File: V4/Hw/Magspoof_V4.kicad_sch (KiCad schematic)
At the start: 35 parts, among them J1 Coil, J2 SWD, P1 USB_C_Plug_USB2.0, Q1 DMG3415U-7, SW1 ON, SW3 S1, SW4 SOURCE MAG, SW5 RESET, U1 CH552G, U2 AP2112K-3.3, U3 TC4424, U5 MCP73831

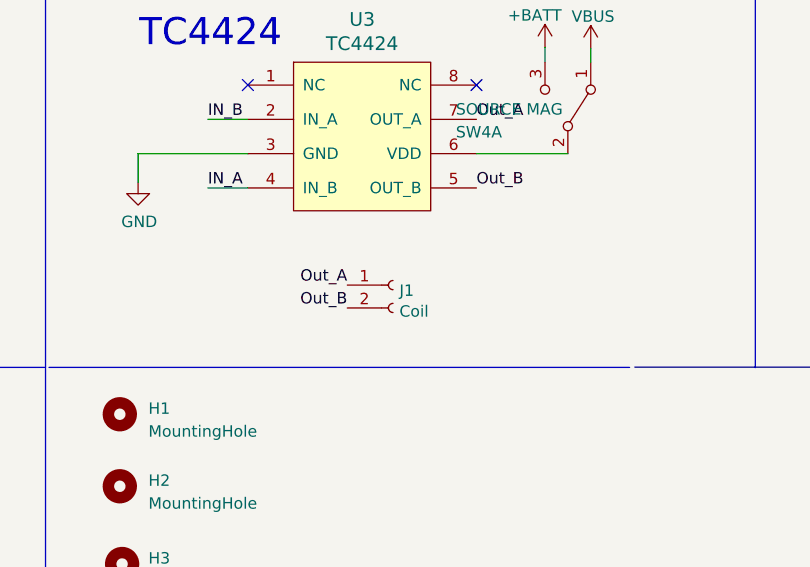
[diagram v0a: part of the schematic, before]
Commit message: feat: flat spiral coil proposals for PCB antenna
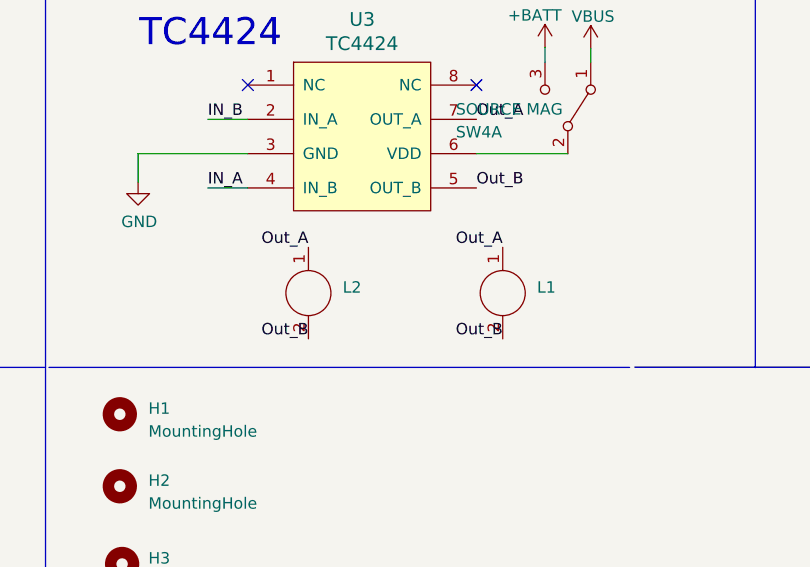
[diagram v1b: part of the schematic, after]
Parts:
- removed J1: Coil, Connector_PinHeader_2.54mm:PinHeader_1x02_P2.54mm_Vertical, symbol Connector:Conn_01x02_Female
- added L1: ~, Library:Coil_20t_35mm_0.2_0.2_0.6_0.3, symbol Magspoof:Coil_20t_35mm_0.2_0.6_0.3
- added L2: ~, magspoof:Coil_25t_30mm_0.2_0.2_0.6_0.3, symbol Magspoof:Coil_20t_35mm_0.2_0.6_0.3
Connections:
- net Out_A: now also L1.1, L2.1
- net Out_B: now also L1.2, L2.2

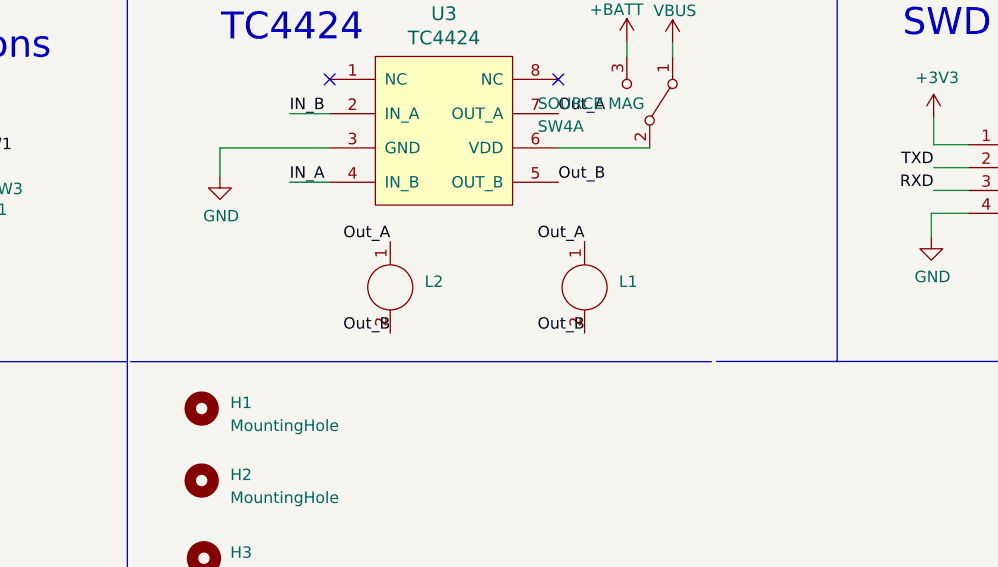
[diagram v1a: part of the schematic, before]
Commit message: feat(hw): add 2 additional coils and the specs of the coils
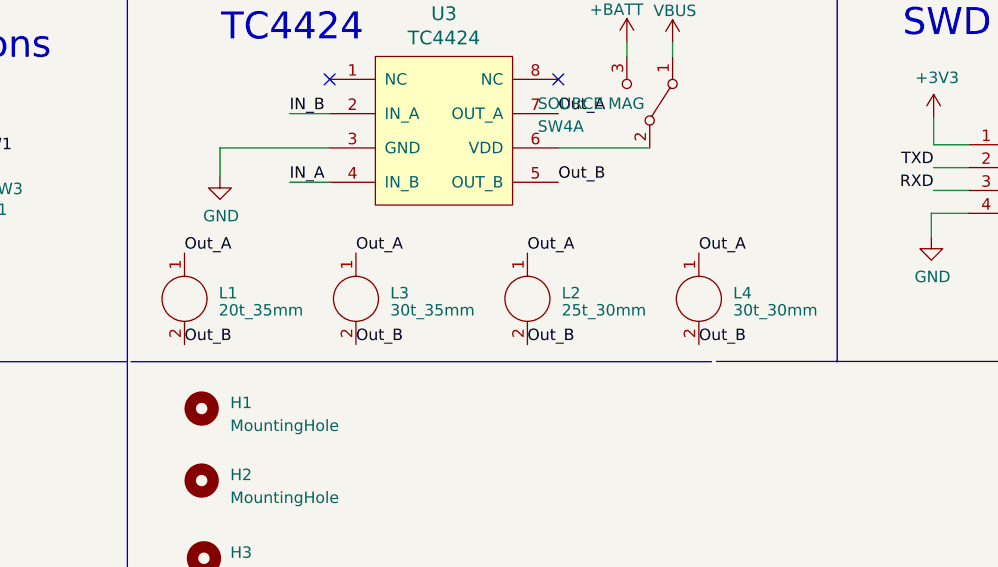
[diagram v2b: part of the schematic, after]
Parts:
- added L3: 30t_35mm, magspoof:Coil_30t_35mm_0.2_0.2_0.6_0.3, symbol Magspoof:Coil_20t_35mm_0.2_0.6_0.3
- added L4: 30t_30mm, magspoof:Coil_30t_30mm_0.2_0.2_0.6_0.3, symbol Magspoof:Coil_20t_35mm_0.2_0.6_0.3
- L1: value ~ -> 20t_35mm
- L2: value ~ -> 25t_30mm
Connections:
- net Out_A: now also L3.1, L4.1
- net Out_B: now also L3.2, L4.2
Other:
- moved on the sheet: L1, L2
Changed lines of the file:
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@@
 	)
 	(label "Out_B"
-		(at 210.82 99.06 180)
+		(at 226.06 100.33 0)
 		(fields_autoplaced yes)
 		(effects
@@
 				(size 1.27 1.27)
 			)
-			(justify right bottom)
+			(justify left bottom)
 		)
 	)
 	(label "Out_A"
-		(at 210.82 88.9 180)
+		(at 226.06 90.17 0)
 		(fields_autoplaced yes)
 		(effects
@@
 				(size 1.27 1.27)
 			)
-			(justify right bottom)
+			(justify left bottom)
 		)
 	)
@@
 	)
 	(label "Out_B"
-		(at 232.41 99.06 180)
+		(at 187.96 100.33 0)
 		(fields_autoplaced yes)
 		(effects
@@
 				(size 1.27 1.27)
 			)
-			(justify right bottom)
+			(justify left bottom)
+		)
+	)
+	(label "Out_A"
+		(at 207.01 90.17 0)
+		(fields_autoplaced yes)
+		(effects
+			(font
+				(size 1.27 1.27)
+			)
+			(justify left bottom)
 		)
 	)
@@
 		)
 	)
+	(label "Out_B"
+		(at 245.11 100.33 0)
+		(fields_autoplaced yes)
+		(effects
+			(font
+				(size 1.27 1.27)
+			)
+			(justify left bottom)
+		)
+	)
+	(label "Out_B"
+		(at 207.01 100.33 0)
+		(fields_autoplaced yes)
+		(effects
+			(font
+				(size 1.27 1.27)
+			)
+			(justify left bottom)
+		)
+	)
 	(label "RXD"
 		(at 271.1958 83.2104 180)
@@
 	)
 	(label "Out_A"
-		(at 232.41 88.9 180)
+		(at 187.96 90.17 0)
 		(fields_autoplaced yes)
 		(effects
@@
 				(size 1.27 1.27)
 			)
-			(justify right bottom)
+			(justify left bottom)
 		)
 	)
@@
 		)
 	)
+	(label "Out_A"
+		(at 245.11 90.17 0)
+		(fields_autoplaced yes)
+		(effects
+			(font
+				(size 1.27 1.27)
+			)
+			(justify left bottom)
+		)
+	)
 	(label "TXD"
 		(at 81.788 91.44 0)
@@
 	(symbol
 		(lib_id "Magspoof:Coil_20t_35mm_0.2_0.6_0.3")
-		(at 214.63 93.98 270)
+		(at 229.87 95.25 270)
 		(unit 1)
 		(exclude_from_sim no)
@@
 		(fields_autoplaced yes)
 		(property "Reference" "L2"
-			(at 214.63 93.3449 90)
+			(at 229.87 94.6149 90)
 			(effects
 				(font
@@
 			)
 		)
-		(property "Value" "~"
-			(at 214.63 95.25 90)
+		(property "Value" "25t_30mm"
+			(at 229.87 96.52 90)
 			(effects
 				(font
@@
 		)
 		(property "Footprint" "magspoof:Coil_25t_30mm_0.2_0.2_0.6_0.3"
-			(at 214.63 93.98 0)
+			(at 229.87 95.25 0)
 			(effects
 				(font
@@
 		)
 		(property "Datasheet" ""
-			(at 214.63 93.98 0)
+			(at 229.87 95.25 0)
 			(effects
 				(font
@@
 		)
 		(property "Description" ""
-			(at 214.63 93.98 0)
+			(at 229.87 95.25 0)
 			(effects
 				(font
@@
 	)
 	(symbol
+		(lib_id "Magspoof:Coil_20t_35mm_0.2_0.6_0.3")
+		(at 248.92 95.25 270)
+		(unit 1)
+		(exclude_from_sim no)
+		(in_bom yes)
+		(on_board yes)
+		(dnp no)
+		(fields_autoplaced yes)
+		(property "Reference" "L4"
+			(at 248.92 94.6149 90)
+			(effects
+				(font
+					(size 1.27 1.27)
+				)
+				(justify left)
+			)
+		)
+		(property "Value" "30t_30mm"
+			(at 248.92 96.52 90)
+			(effects
+				(font
+					(size 1.27 1.27)
+				)
+				(justify left)
+			)
+		)
+		(property "Footprint" "magspoof:Coil_30t_30mm_0.2_0.2_0.6_0.3"
+			(at 248.92 95.25 0)
+			(effects
+				(font
+					(size 1.27 1.27)
+				)
+				(hide yes)
+			)
+		)
+		(property "Datasheet" ""
+			(at 248.92 95.25 0)
+			(effects
+				(font
+					(size 1.27 1.27)
+				)
+				(hide yes)
+			)
+		)
+		(property "Description" ""
+			(at 248.92 95.25 0)
+			(effects
+				(font
+					(size 1.27 1.27)
+				)
+				(hide yes)
+			)
+		)
+		(pin "2"
+		)
+		(pin "1"
+		)
+		(instances
+			(project "Magspoof_V4"
+				(path "/a54f9b8d-da56-4b4b-9f0d-04fac56db24a"
+					(reference "L4")
+					(unit 1)
+				)
+			)
+		)
+	)
+	(symbol
 		(lib_id "power:GND")
 		(at 55.88 39.243 0)
@@
 	)
 	(symbol
+		(lib_id "Magspoof:Coil_20t_35mm_0.2_0.6_0.3")
+		(at 210.82 95.25 270)
+		(unit 1)
+		(exclude_from_sim no)
+		(in_bom yes)
+		(on_board yes)
+		(dnp no)
+		(fields_autoplaced yes)
+		(property "Reference" "L3"
+			(at 210.82 94.6149 90)
+			(effects
+				(font
+					(size 1.27 1.27)
+				)
+				(justify left)
+			)
+		)
+		(property "Value" "30t_35mm"
+			(at 210.82 96.52 90)
+			(effects
+				(font
+					(size 1.27 1.27)
+				)
+				(justify left)
+			)
+		)
+		(property "Footprint" "magspoof:Coil_30t_35mm_0.2_0.2_0.6_0.3"
+			(at 210.82 95.25 0)
+			(effects
+				(font
+					(size 1.27 1.27)
+				)
+				(hide yes)
+			)
+		)
+		(property "Datasheet" ""
+			(at 210.82 95.25 0)
+			(effects
+				(font
+					(size 1.27 1.27)
+				)
+				(hide yes)
+			)
+		)
+		(property "Description" ""
+			(at 210.82 95.25 0)
+			(effects
+				(font
+					(size 1.27 1.27)
+				)
+				(hide yes)
+			)
+		)
+		(pin "2"
+		)
+		(pin "1"
+		)
+		(instances
+			(project "Magspoof_V4"
+				(path "/a54f9b8d-da56-4b4b-9f0d-04fac56db24a"
+					(reference "L3")
+					(unit 1)
+				)
+			)
+		)
+	)
+	(symbol
 		(lib_id "Device:R")
 		(at 147.32 43.053 0)
@@
 	(symbol
 		(lib_id "Magspoof:Coil_20t_35mm_0.2_0.6_0.3")
-		(at 236.22 93.98 270)
+		(at 191.77 95.25 270)
 		(unit 1)
 		(exclude_from_sim no)
@@
 		(on_board yes)
 		(dnp no)
-		(fields_autoplaced yes)
 		(property "Reference" "L1"
-			(at 236.22 93.3449 90)
+			(at 191.77 94.6149 90)
 			(effects
 				(font
@@
 			)
 		)
-		(property "Value" "~"
-			(at 236.22 95.25 90)
+		(property "Value" "20t_35mm"
+			(at 191.77 96.52 90)
 			(effects
 				(font
@@
 		)
 		(property "Footprint" "Library:Coil_20t_35mm_0.2_0.2_0.6_0.3"
-			(at 236.22 93.98 0)
+			(at 180.594 95.504 0)
 			(effects
 				(font
@@
 		)
 		(property "Datasheet" ""
-			(at 236.22 93.98 0)
+			(at 191.77 95.25 0)
 			(effects
 				(font
@@
 		)
 		(property "Description" ""
-			(at 236.22 93.98 0)
+			(at 191.77 95.25 0)
 			(effects
 				(font
